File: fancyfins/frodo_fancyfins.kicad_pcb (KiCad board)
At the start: 2 copper layers, 4.6 x 6.4 mm, 100 parts, among them J1 TC2050, J4 SWD Header, J5 CFG Header, U10 L78L05_SOT89, U11 L78L05_SOT89, U12 L78L05_SOT89, U13 L78L05_SOT89, U14 L78L05_SOT89, U15 L78L05_SOT89, U16 AZ1117-5.0, U17 W25Q128JVP, U18 L78L05_SOT89, U2 MCP2562-E-SN, U3 AZ1117-3.3, U4 STM32F103RCTx, U7 L78L05_SOT89, U8 L78L05_SOT89, U9 L78L05_SOT89, Y1 8MHz 12pF

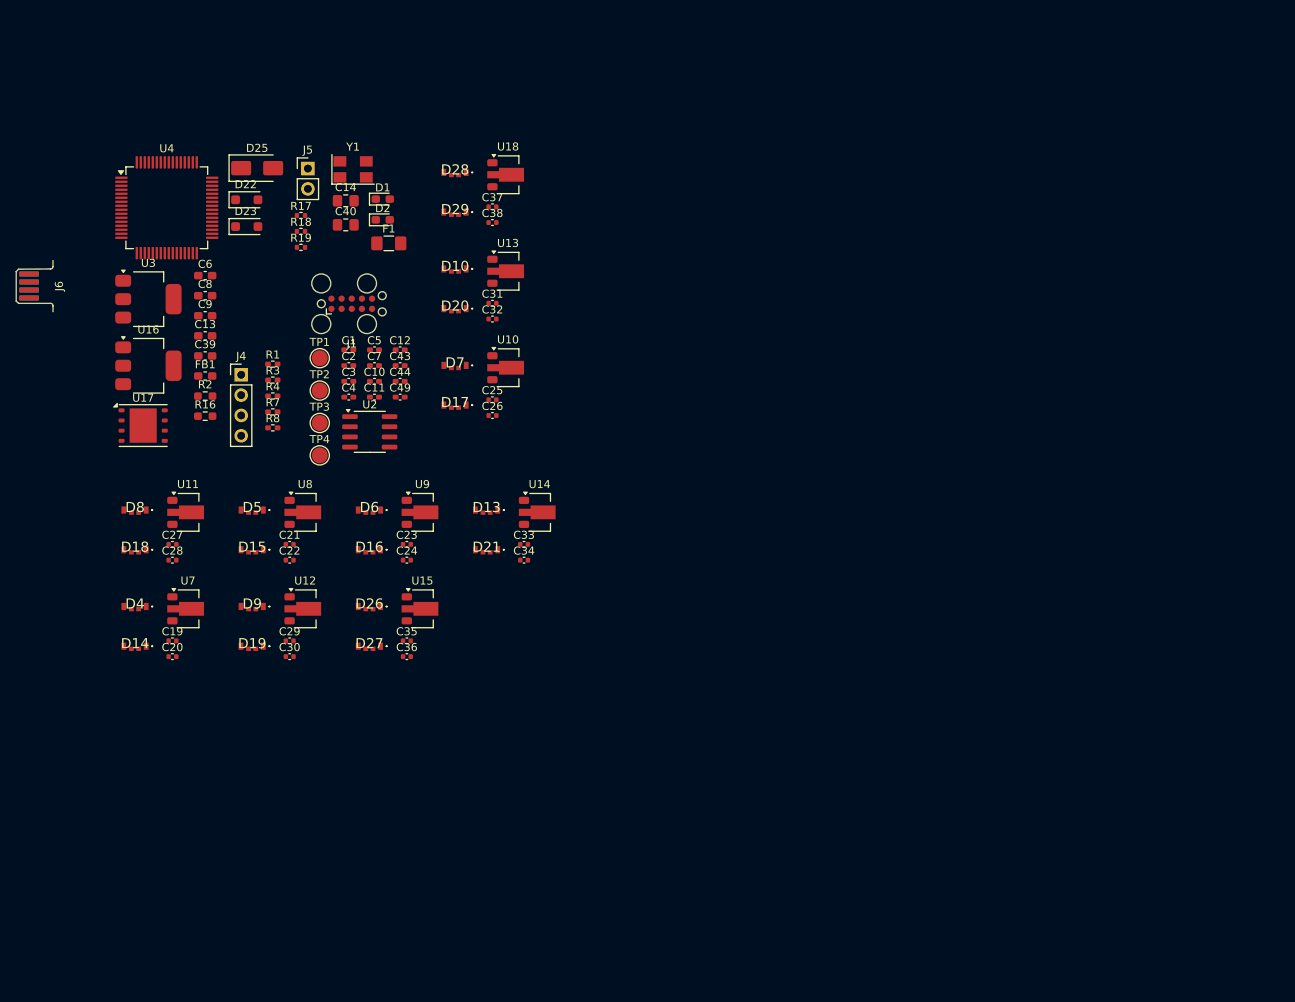
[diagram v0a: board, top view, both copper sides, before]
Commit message: finished layout, added a bunch of footprints, fixed outer form
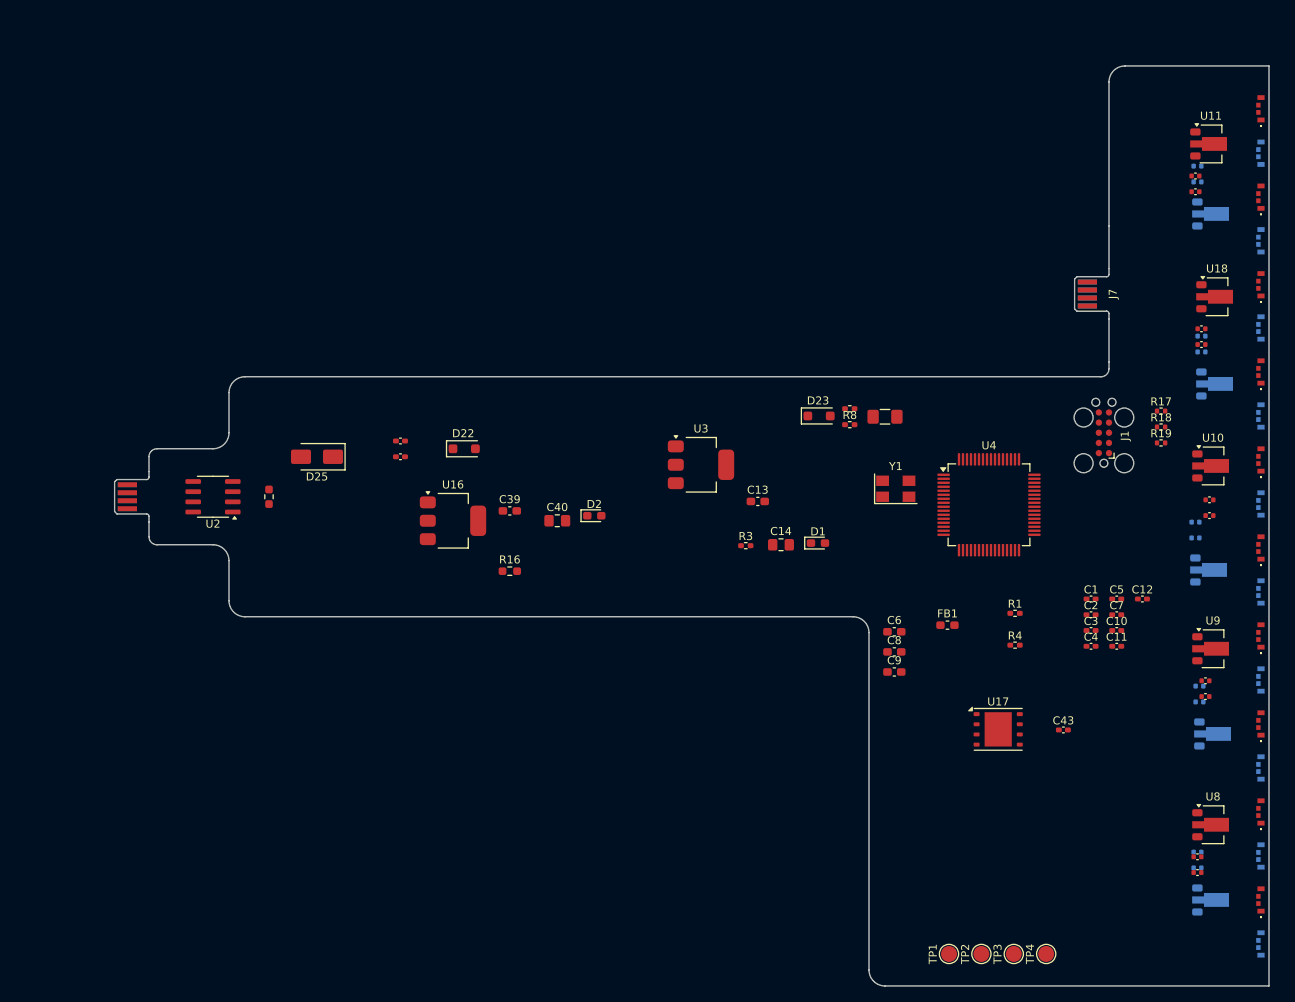
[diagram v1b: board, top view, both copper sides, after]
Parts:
- removed J4: SWD Header, Connector_PinHeader_2.54mm:PinHeader_1x04_P2.54mm_Vertical
- removed J5: CFG Header, Connector_PinHeader_2.54mm:PinHeader_1x02_P2.54mm_Vertical
- added J7: ~, fancyfins:card_edge_connector_2x4, F.Cu at (205.0, 63.5)
- C19, C20, C29, C30, C31, C32, C33, C34, C35, C36, D10, D13, D14, D19, D20, D21, D26, D27, D4, D9, J6, U12, U13, U14, U15, U7: moved to B.Cu
- moved D14 153.7 mm to (224.0, 45.9), turned to 90 degrees
- moved D8 149.4 mm to (224.0, 40.4), turned to -90 degrees
- moved D4 148.0 mm to (224.0, 56.9), turned to 90 degrees
- moved D18 147.5 mm to (224.0, 51.4), turned to -90 degrees
- moved C20 142.0 mm to (216.1, 47.5)
- moved C19 140.4 mm to (216.1, 49.5)
- moved U7 137.3 mm to (218.0, 53.5)
- moved C27 135.9 mm to (215.8, 48.8)
- moved C28 135.9 mm to (215.8, 50.7)
- moved U11 135.9 mm to (217.8, 44.8)
- moved D15 133.5 mm to (224.0, 139.2), turned to -90 degrees
- moved D9 133.0 mm to (224.0, 144.8), turned to 90 degrees
- moved D5 131.6 mm to (224.0, 128.2), turned to -90 degrees
- moved D19 128.8 mm to (224.0, 133.8), turned to 90 degrees
- moved C21 120.0 mm to (216.1, 133.9)
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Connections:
- R2 pad 1: CAN_1_H -> CAN_H_IN
- R2 pad 2: CAN_1_L -> CAN_L_IN
- U2 pad 6: CAN_1_L -> CAN_L_IN
- U2 pad 7: CAN_1_H -> CAN_H_IN
- U4 pad 29: unconnected-(U4-PB10-Pad29) -> P_SCL
- U4 pad 30: unconnected-(U4-PB11-Pad30) -> P_SDA
- U4 pad 39: RST_RADIO -> unconnected-(U4-PC8-Pad39)
- U4 pad 40: BSY_RADIO -> unconnected-(U4-PC9-Pad40)
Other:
- board size 4.6 x 6.4 mm -> 140 x 115 mm

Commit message: changed fancyfins layout a bit; added local footprint library
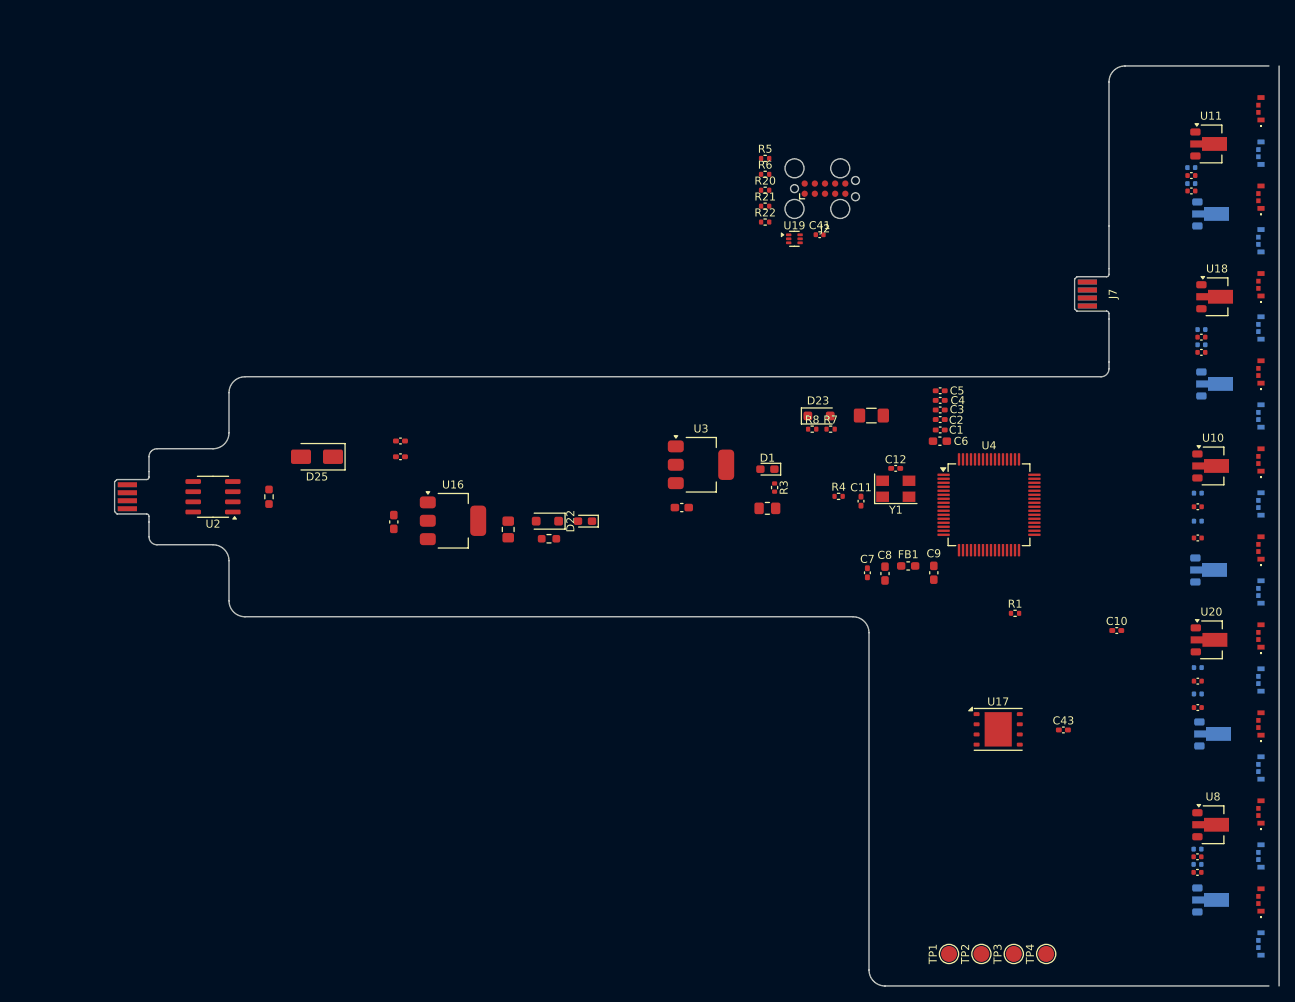
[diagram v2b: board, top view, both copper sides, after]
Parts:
- removed C23: 330n, Capacitor_SMD:C_0402_1005Metric
- removed C24: 100n, Capacitor_SMD:C_0402_1005Metric
- removed D16, D6: 3210, fancyfins:1313210530000
- removed J1: TC2050, Connector:Tag-Connect_TC2050-IDC-FP_2x05_P1.27mm_Vertical
- removed R17, R18, R19: 22, Resistor_SMD:R_0402_1005Metric
- removed U9: L78L05_SOT89, Package_TO_SOT_SMD:SOT-89-3
- added C41: 100n, Capacitor_SMD:C_0402_1005Metric, F.Cu at (168.8, 56.1)
- added C42: 330n, Capacitor_SMD:C_0402_1005Metric, F.Cu at (216.1, 111.9)
- added C45: 100n, Capacitor_SMD:C_0402_1005Metric, F.Cu at (216.1, 115.2)
- added D30: 3210, fancyfins:1313210530000, F.Cu at (224.0, 106.2)
- added D31: 3210, fancyfins:1313210530000, F.Cu at (224.0, 117.2)
- added J2: TC2050, Connector:Tag-Connect_TC2050-IDC-FP_2x05_P1.27mm_Vertical, F.Cu at (169.5, 50.3)
- added R20: 22, Resistor_SMD:R_0402_1005Metric, F.Cu at (162.0, 50.5)
- added R21: 22, Resistor_SMD:R_0402_1005Metric, F.Cu at (162.0, 52.5)
- added R22: 22, Resistor_SMD:R_0402_1005Metric, F.Cu at (162.0, 54.5)
- added R5: 10k, Resistor_SMD:R_0402_1005Metric, F.Cu at (162.0, 46.6)
- added R6: 10k, Resistor_SMD:R_0402_1005Metric, F.Cu at (162.0, 48.5)
- added U19: TPD4E1U06, Package_TO_SOT_SMD:SOT-563, F.Cu at (165.7, 56.6)
- added U20: L78L05_SOT89, Package_TO_SOT_SMD:SOT-89-3, F.Cu at (217.8, 106.7)
- C26: moved to B.Cu
- C34: moved to F.Cu
- R1, R3, R4, R7, R8: footprint Resistor_SMD:R_0402_1005Metric_Pad0.72x0.64mm_HandSolder -> Resistor_SMD:R_0402_1005Metric
- moved C11 36.8 mm to (174.0, 89.4), turned to -90 degrees
- moved C4 36.1 mm to (183.9, 76.8), turned to 180 degrees
- moved C12 34.9 mm to (178.3, 85.3), turned to 180 degrees
- moved C5 34.1 mm to (183.9, 75.6), turned to 180 degrees
- moved C3 33.4 mm to (183.9, 78.0), turned to 180 degrees
- moved C7 31.6 mm to (174.8, 98.3), turned to -90 degrees
- moved C2 30.8 mm to (183.9, 79.2), turned to 180 degrees
- moved R4 28.9 mm to (171.2, 88.8)
- moved C1 28.3 mm to (183.9, 80.5), turned to 180 degrees
- moved C6 24.5 mm to (183.9, 81.9), turned to 180 degrees
- moved C39 14.6 mm to (115.6, 92.0), turned to 90 degrees
- moved D22 13.8 mm to (134.8, 91.9), turned to 180 degrees
- moved C9 13.3 mm to (183.1, 98.3), turned to -90 degrees
- moved D1 11.2 mm to (162.3, 85.4), turned to 180 degrees
- moved C8 9.86 mm to (177.0, 98.5), turned to -90 degrees
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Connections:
- D10 pad 4: /LED_grouped5/DO -> /LED_grouped6/DIN
- D13 pad 4: /LED_grouped6/DO -> /LED_grouped3/DO
- D18 pad 4: /LED_grouped4/DO -> /LED_grouped/DIN
- D20 pad 4: /LED_grouped6/DO -> /LED_grouped3/DIN
- D21 pad 4: /LED_grouped7/DO -> /LED_grouped2/DIN
- D26 pad 4: /LED_grouped7/DO -> /LED_grouped2/DO
- D27 pad 4: /LED_grouped8/DO -> /LED_grouped1/DIN
- D28 pad 4: /LED_grouped8/DO -> /LED_grouped/DO
- D29 pad 4: /LED_grouped9/DO -> /LED_grouped6/DIN
- D4 pad 4: LED_Signal -> /LED_grouped/DIN
- D5 pad 4: /LED_grouped/DO -> /LED_grouped1/DIN
- D7 pad 4: /LED_grouped2/DO -> /LED_grouped3/DIN
- D8 pad 4: /LED_grouped3/DO -> LED_Signal
- D9 pad 4: /LED_grouped4/DO -> /LED_grouped1/DO
- U17 pad 9: (no net) -> unconnected-(U17-GND-Pad9)
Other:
- board size 140 x 115 mm -> 141.3 x 115 mm

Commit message: added fancy fins routing
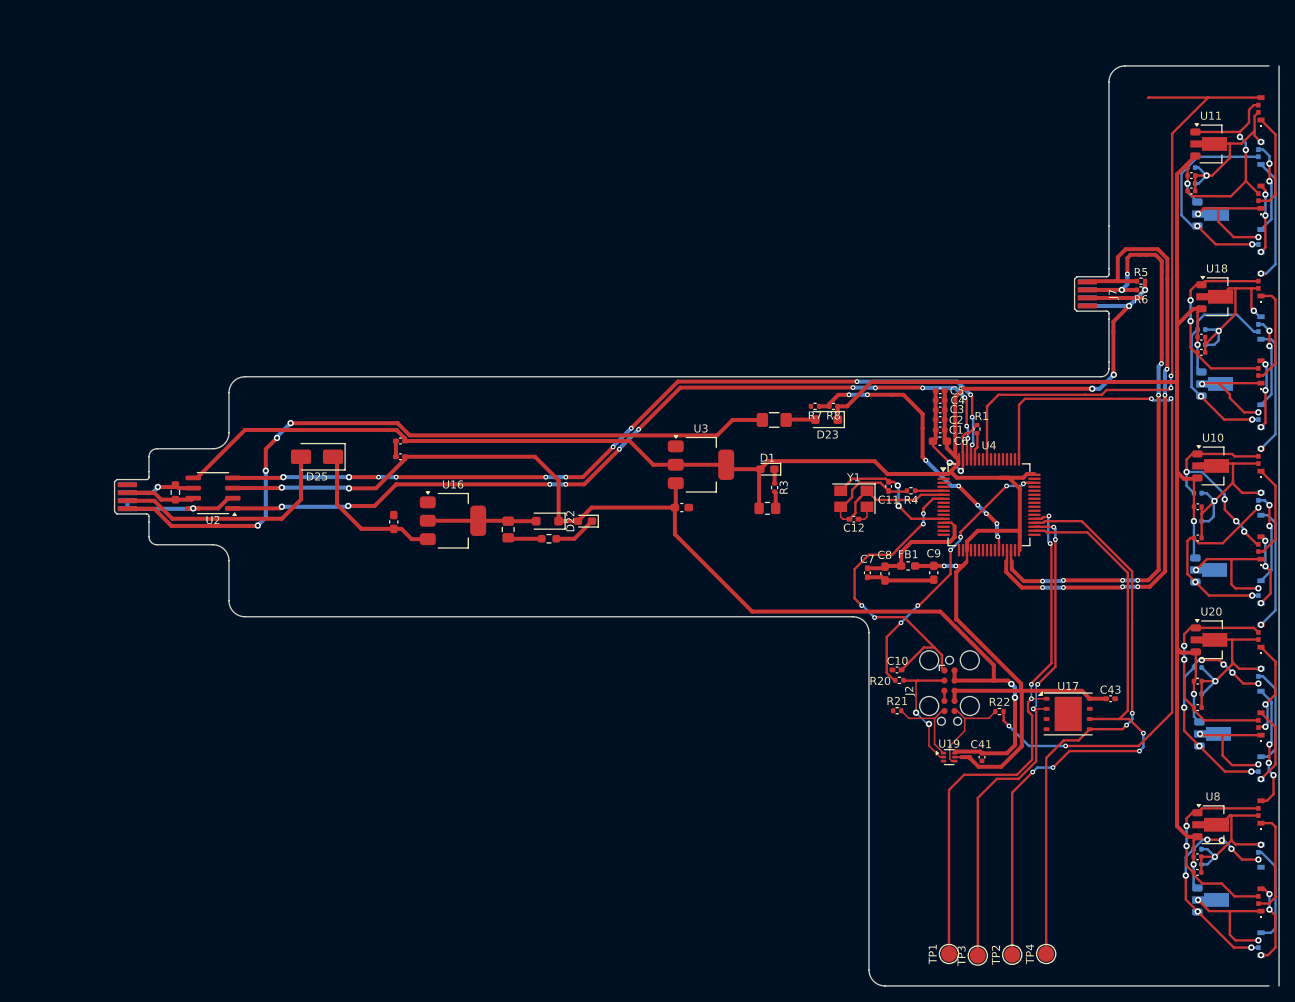
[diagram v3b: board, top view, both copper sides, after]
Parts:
- moved C41 68.4 mm to (189.1, 121.4), turned to 90 degrees
- moved R22 67.8 mm to (191.3, 115.7)
- moved U19 67.6 mm to (185.0, 121.4)
- moved R21 65.2 mm to (178.5, 115.6)
- moved J2 64.7 mm to (185.1, 113.1), turned to -90 degrees
- moved R20 63.5 mm to (178.8, 111.8)
- moved R5 49.4 mm to (209.0, 61.9), turned to 180 degrees
- moved R6 49.2 mm to (209.0, 63.0), turned to 180 degrees
- moved C10 27.9 mm to (178.5, 110.5), turned to 180 degrees
- moved R1 23.5 mm to (188.5, 80.4), turned to -90 degrees
- moved F1 12.2 mm to (163.2, 79.2), turned to 0 degrees
- moved R2 11.7 mm to (88.3, 88.3)
- moved R4 9.08 mm to (180.2, 88.1), turned to 180 degrees
- moved U17 8.96 mm to (199.9, 116.0)
- moved C12 8.22 mm to (173.1, 91.7), turned to 0 degrees
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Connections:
- U4 pad 10: SG_REF -> unconnected-(U4-PC2-Pad10)
- U4 pad 11: SG_VOUT1 -> unconnected-(U4-PC3-Pad11)
- U4 pad 17: DIO1_RADIO -> unconnected-(U4-PA3-Pad17)
- U4 pad 20: DIO3_RADIO -> unconnected-(U4-PA4-Pad20)
- U4 pad 21: SPI1_SCK -> unconnected-(U4-PA5-Pad21)
- U4 pad 22: SPI1_MISO -> unconnected-(U4-PA6-Pad22)
- U4 pad 23: SPI1_MOSI -> unconnected-(U4-PA7-Pad23)
- U4 pad 24: SPI_CS_RADIO -> unconnected-(U4-PC4-Pad24)
- U4 pad 26: TH_sense -> unconnected-(U4-PB0-Pad26)
- U4 pad 41: CAN_ADDR0 -> unconnected-(U4-PA8-Pad41)
- U4 pad 42: CAN_ADDR1 -> unconnected-(U4-PA9-Pad42)
- U4 pad 8: SG_EN -> unconnected-(U4-PC0-Pad8)
- U4 pad 9: SG_VOUT0 -> unconnected-(U4-PC1-Pad9)
- Y1 pad 1: Net-(C11-Pad1) -> OSC_OUT
- Y1 pad 3: OSC_OUT -> Net-(C11-Pad1)
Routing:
- net GND: track 0.00 -> 288.4 mm, vias 0 -> 25
- net +3.3V: track 0.00 -> 261.1 mm, vias 0 -> 6
- net VD: track 0.00 -> 183.8 mm, vias 0 -> 5
- net +5V: track 0.00 -> 143.6 mm, vias 0 -> 4
- net CAN_TX: track 0.00 -> 106.3 mm, vias 0 -> 12
- net CAN_RX: track 0.00 -> 106.3 mm, vias 0 -> 12
- net charging_voltage: track 0.00 -> 92.1 mm, vias 0 -> 4
- net SWCLK: track 0.00 -> 90.9 mm, vias 0 -> 4
- net SPI2_SCK: track 0.00 -> 84.6 mm, vias 0 -> 4
- net LED_Signal: track 0.00 -> 82.9 mm, vias 0 -> 2
- net P_SCL: track 0.00 -> 80.0 mm, vias 0 -> 6
- net P_SDA: track 0.00 -> 76.2 mm, vias 0 -> 8
- net SPI2_MOSI: track 0.00 -> 71.8 mm, vias 0 -> 2
- net SPI_CS_FLASH: track 0.00 -> 68.7 mm, vias 0 -> 4
- net SPI2_MISO: track 0.00 -> 63.9 mm, vias 0 -> 4
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
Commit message: fixed some errors in the fancyfins pcb
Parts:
- moved C6 18.5 mm to (195.9, 95.9), turned to 0 degrees
- moved C5 15.8 mm to (196.4, 85.2), turned to 0 degrees
- moved C4 10.0 mm to (181.8, 86.6), turned to -90 degrees
- moved D25 9.05 mm to (106.3, 92.9)
- moved C3 8.66 mm to (182.8, 86.6), turned to -90 degrees
- moved C2 2.68 mm to (185.2, 81.5)
- moved C1 2.43 mm to (185.2, 82.5)
- moved D10 1.28 mm to (222.7, 79.0)
- moved D13 1.28 mm to (222.7, 101.0)
- moved D15 1.28 mm to (222.7, 139.5)
- moved D17 1.28 mm to (222.7, 95.5)
- moved D19 1.28 mm to (222.7, 134.0)
- moved D20 1.28 mm to (222.7, 68.0)
- moved D21 1.28 mm to (222.7, 90.0)
- moved D26 1.28 mm to (222.7, 123.0)
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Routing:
- net GND: track 288.4 -> 211.1 mm, vias 25 -> 54
- net LED_Signal: track 82.9 -> 74.1 mm
- net v_main: track 19.3 -> 12.1 mm
- net +3.3V: track 261.1 -> 254.5 mm, vias 6 -> 4
- net Net-(D25-A): track 29.0 -> 23.5 mm
- net P_SDA: track 76.2 -> 73.7 mm
- net P_SCL: track 80.0 -> 77.5 mm
- net SPI_CS_FLASH: track 68.7 -> 67.0 mm
- net CAN_TX: track 106.3 -> 107.8 mm, vias 12 -> 10
- net SPI2_MISO: track 63.9 -> 62.5 mm
- net SWCLK: track 90.9 -> 89.5 mm, vias 4 -> 6
- net SPI2_SCK: track 84.6 -> 83.2 mm
- net VD: track 183.8 -> 182.5 mm
- net SWDIO: track 34.8 -> 35.6 mm, vias 6 -> 4
- net /LED_grouped3/DO: track 9.31 -> 9.90 mm
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- added copper zone on B.Cu, net GND
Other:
- board size 141.3 x 115 mm -> 140 x 115 mm

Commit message: fixed led symbol
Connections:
- D14 pad 1: GND -> /LED_grouped/DO
- D14 pad 2: Net-(D14-DIN) -> GND
- D14 pad 4: /LED_grouped/DO -> Net-(D14-DO)
- D15 pad 1: GND -> /LED_grouped1/DO
- D15 pad 2: Net-(D15-DIN) -> GND
- D15 pad 4: /LED_grouped1/DO -> Net-(D15-DO)
- D17 pad 1: GND -> /LED_grouped3/DO
- D17 pad 2: Net-(D17-DIN) -> GND
- D17 pad 4: /LED_grouped3/DO -> Net-(D17-DO)
- D18 pad 1: GND -> /LED_grouped/DIN
- D18 pad 2: Net-(D18-DIN) -> GND
- D18 pad 4: /LED_grouped/DIN -> Net-(D18-DIN)
- D19 pad 1: GND -> /LED_grouped5/DO
- D19 pad 2: Net-(D19-DIN) -> GND
- D19 pad 4: /LED_grouped5/DO -> Net-(D19-DO)
- D20 pad 1: GND -> /LED_grouped3/DIN
- D20 pad 2: Net-(D10-DO) -> GND
- D20 pad 4: /LED_grouped3/DIN -> Net-(D10-DO)
- D21 pad 1: GND -> /LED_grouped2/DIN
- D21 pad 2: Net-(D13-DO) -> GND
- D21 pad 4: /LED_grouped2/DIN -> Net-(D13-DO)
- D27 pad 1: GND -> /LED_grouped1/DIN
- D27 pad 2: Net-(D26-DO) -> GND
- D27 pad 4: /LED_grouped1/DIN -> Net-(D26-DO)
- D29 pad 1: GND -> /LED_grouped6/DIN
- D29 pad 2: Net-(D28-DO) -> GND
- D29 pad 4: /LED_grouped6/DIN -> Net-(D28-DO)
- D31 pad 1: GND -> /LED_grouped2/DO
- D31 pad 2: Net-(D30-DO) -> GND
- D31 pad 4: /LED_grouped2/DO -> Net-(D30-DO)
- D4 pad 1: Net-(D14-DIN) -> Net-(D14-DO)
- D5 pad 1: Net-(D15-DIN) -> Net-(D15-DO)
- D7 pad 1: Net-(D17-DIN) -> Net-(D17-DO)
- D9 pad 1: Net-(D19-DIN) -> Net-(D19-DO)
- U17 pad 9: unconnected-(U17-GND-Pad9) -> GND
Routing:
- net GND: track 211.1 -> 260.3 mm, vias 54 -> 56
- net Net-(D15-DIN): track 13.0 -> 0.00 mm
- net Net-(D19-DIN): track 12.6 -> 0.00 mm
- net Net-(D17-DIN): track 12.0 -> 0.00 mm
- net Net-(D14-DIN): track 11.6 -> 0.00 mm, vias 2 -> 0

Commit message: changed fancyfinns pcb layout
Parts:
- removed D22: D_Schottky, Diode_SMD:D_SOD-123F
- moved D23 66.8 mm to (105.5, 97.3)
- moved R8 66.6 mm to (106.5, 95.6)
- moved R7 66.3 mm to (104.5, 95.6)
- moved F1 65.0 mm to (100.8, 97.3)
- moved TP1 57.7 mm to (200.1, 90.3)
- moved TP3 54.0 mm to (200.2, 93.4)
- moved TP4 48.8 mm to (202.4, 97.5)
- moved TP2 46.4 mm to (202.4, 100.7)
- moved D2 23.8 mm to (115.9, 88.5), turned to -90 degrees
- moved U17 23.7 mm to (205.4, 92.9)
- moved C43 22.8 mm to (209.2, 91.6), turned to 90 degrees
- moved R3 20.4 mm to (182.7, 81.5)
- moved U3 20.2 mm to (173.9, 81.6)
- moved C13 20.0 mm to (171.2, 86.0), turned to 180 degrees
- moved C14 19.6 mm to (180.2, 82.3)
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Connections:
- C40 pad 1: Net-(D22-A) -> +5V
- U16 pad 2: Net-(D22-A) -> +5V
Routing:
- net +3.3V: track 254.5 -> 0.00 mm, vias 4 -> 0
- net GND: track 260.3 -> 86.0 mm, vias 56 -> 26
- net +5V: track 143.4 -> 0.00 mm, vias 2 -> 0
- net VD: track 182.5 -> 41.4 mm
- net CAN_TX: track 107.8 -> 0.00 mm, vias 10 -> 0
- net CAN_RX: track 106.3 -> 0.00 mm, vias 10 -> 0
- net charging_voltage: track 92.1 -> 0.00 mm, vias 4 -> 0
- net SWCLK: track 89.5 -> 0.00 mm, vias 6 -> 0
- net SPI2_SCK: track 83.2 -> 0.00 mm, vias 4 -> 0
- net P_SCL: track 77.5 -> 0.00 mm, vias 6 -> 0
- net P_SDA: track 73.7 -> 0.00 mm, vias 8 -> 0
- net SPI2_MOSI: track 71.8 -> 0.00 mm, vias 2 -> 0
- net SPI_CS_FLASH: track 67.0 -> 0.00 mm, vias 4 -> 0
- net SPI2_MISO: track 62.5 -> 0.00 mm, vias 4 -> 0
- net LED_Signal: track 74.1 -> 13.0 mm, vias 2 -> 0
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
